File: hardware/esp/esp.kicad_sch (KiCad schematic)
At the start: 41 parts, among them J1 USB_C_Receptacle_USB2.0_16P, J2 Conn_01x02, J3 USB_C_Receptacle_USB2.0_16P, J4 Conn_01x02, Q1 PNP, Q2 PNP, Q3 PNP, Q4 PNP, SW1 RESET, SW2 BOOT, U1 AMS1117-3.3, U2 ESP32-S3-WROOM-1, U6 CP2102N-Axx-xQFN20

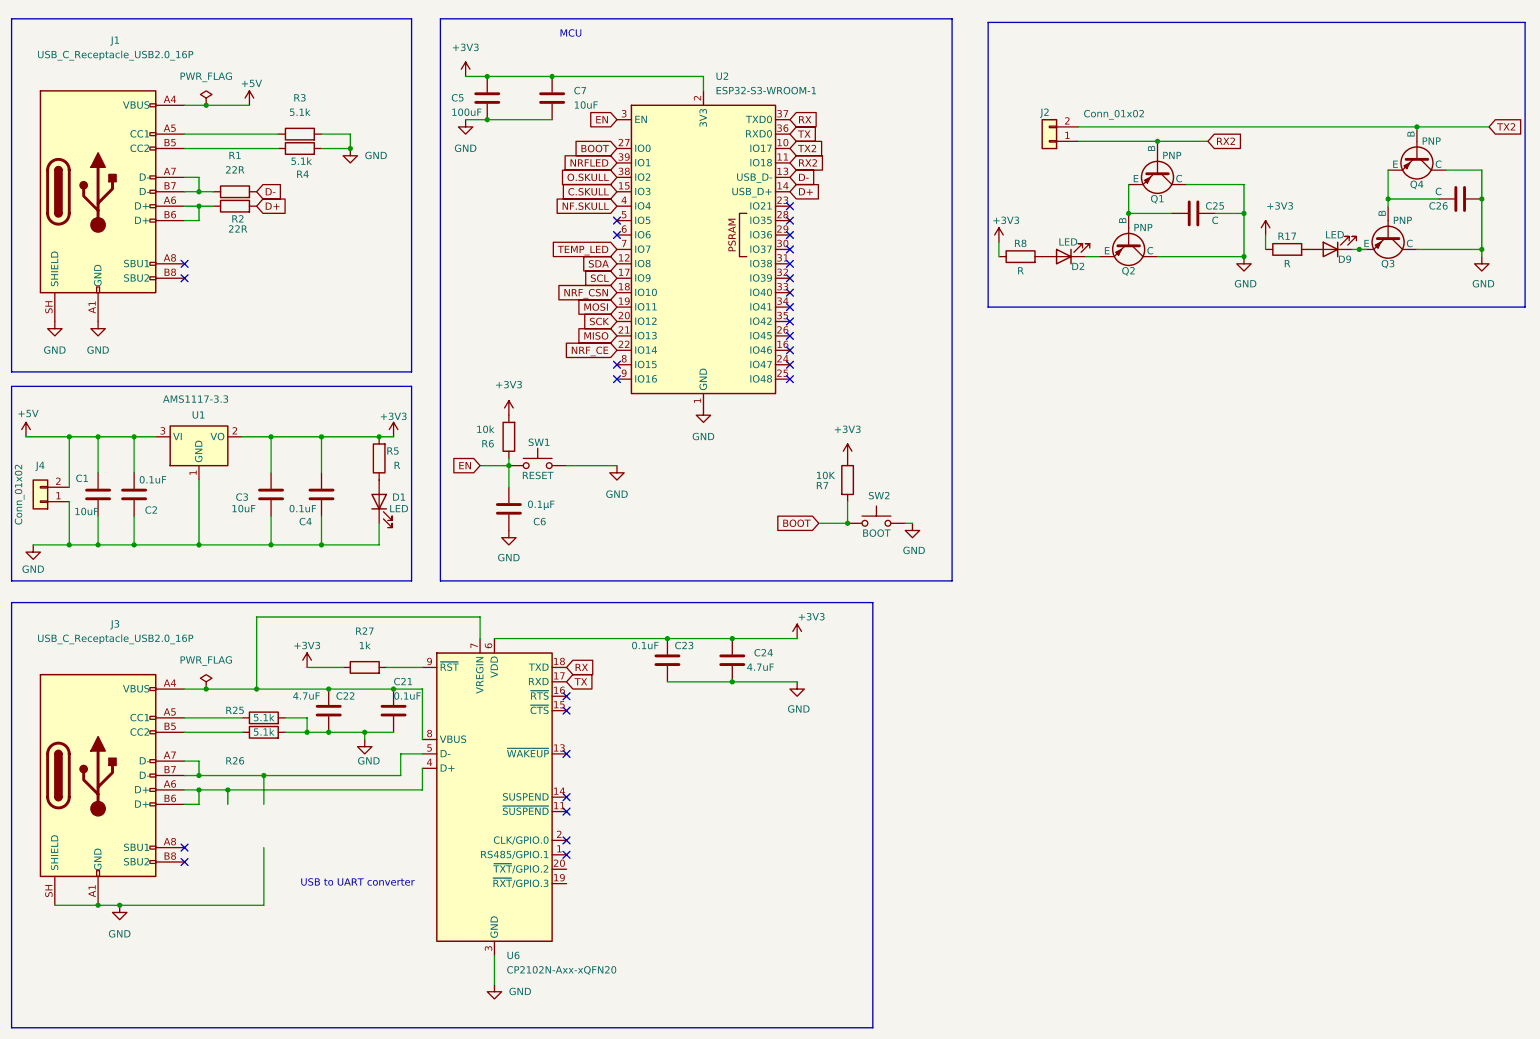
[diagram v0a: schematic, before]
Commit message: Placing Bidirectional TVS diodes and fixing schematic + placing components on pcb
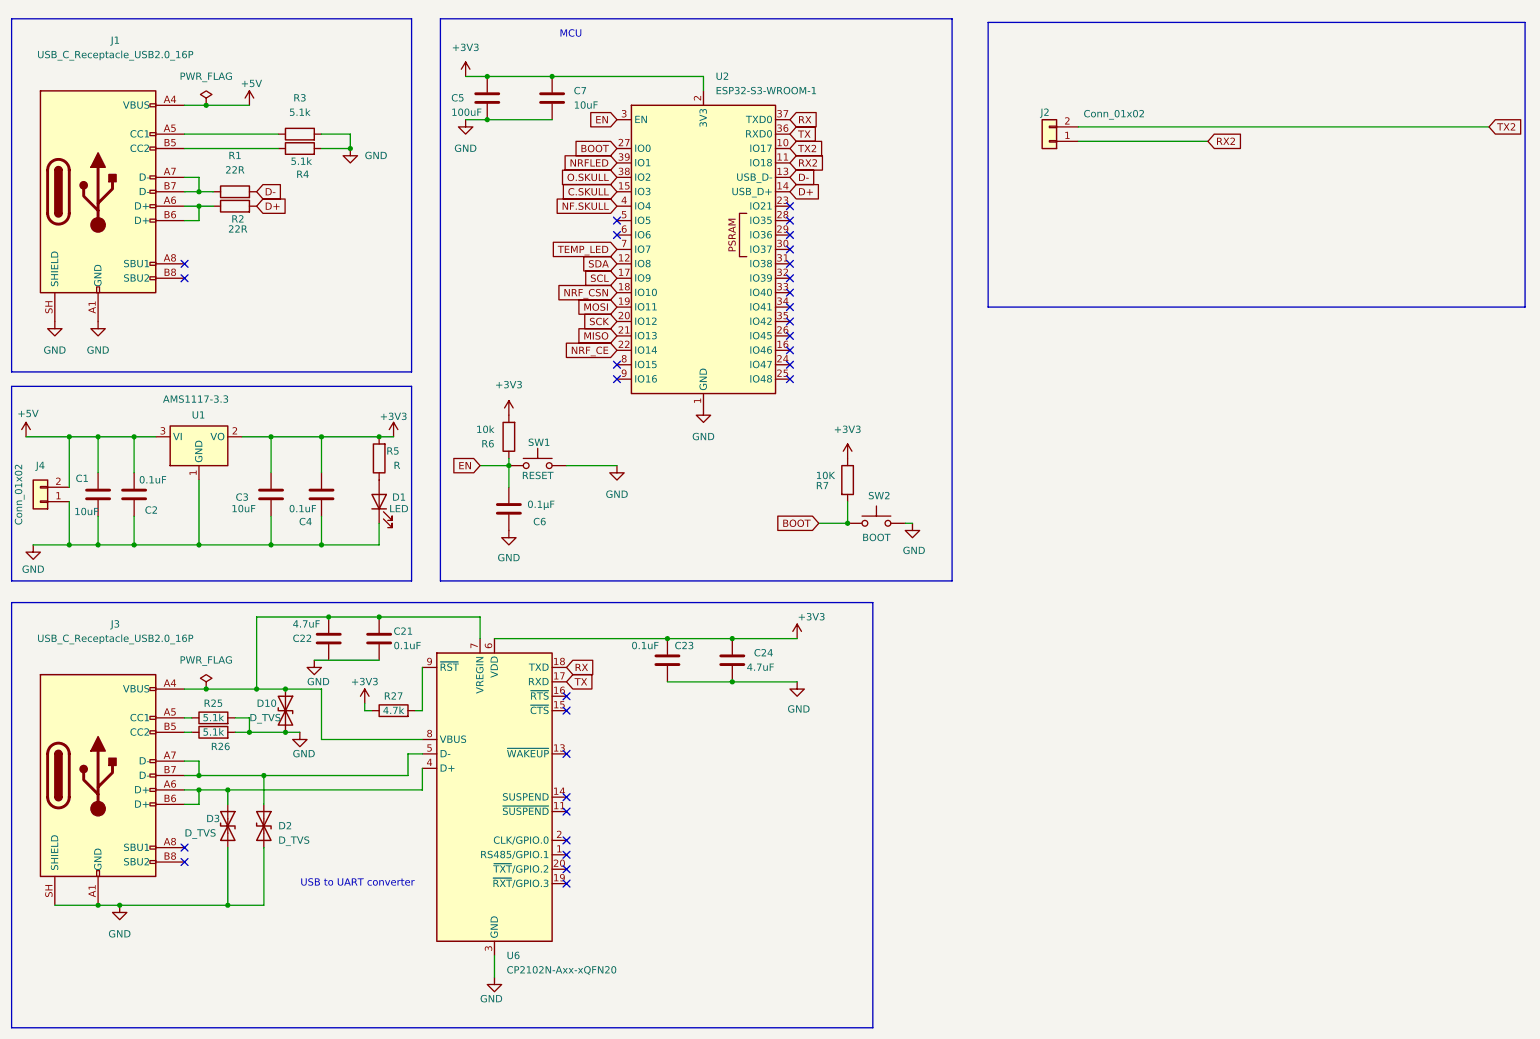
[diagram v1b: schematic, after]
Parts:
- removed C25, C26: C, Capacitor_SMD:C_0805_2012Metric, symbol Device:C
- removed D2, D9: LED, LED_SMD:LED_0603_1608Metric, symbol Device:LED
- removed Q1, Q2, Q3, Q4: PNP, symbol Simulation_SPICE:PNP
- removed R17, R8: R, Resistor_SMD:R_0805_2012Metric, symbol Device:R
- added D10, D2, D3: D_TVS, Diode_SMD:D_SOD-123, symbol Device:D_TVS
- R27: value 1k -> 4.7k
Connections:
- net GND: now also D10.2 (A2), D2.2 (A2), D3.2 (A2); no longer C22.2
- net at C21.1, C22.1, J3.A4 (VBUS)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: now also D10.1 (A1)
- net at J3.A6 (D+), J3.B6 (D+), U6.4 (D+): now also D3.1 (A1)
- net at J3.A7 (D-), J3.B7 (D-), U6.5 (D-): now also D2.1 (A1)
- no-connect marks 28 -> 30
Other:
- moved on the sheet: C21, C22, R25, R26, R27

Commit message: Updating pins, and scehmatic
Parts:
- renumbered C23 to C10, C24 to C11, C22 to C5, C21 to C6, C5 to C7, C6 to C8, C7 to C9, D3 to D1, D10 to D3, D1 to D4, J4 to J1, J1 to J2, J2 to J4, R25 to R1, R7 to R10, R26 to R2, R1 to R3, R2 to R4, R3 to R5, R4 to R6, R5 to R7, R27 to R8, R6 to R9, U6 to U2, U2 to U3
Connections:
- net GND is gone; now on net +3V3: C1.2, C10.2, C11.2, C2.2, C3.2, C4.2, C6.2, C7.1, C8.1, C9.1, D1.2 (A2), D2.2 (A2), D3.2 (A2), D4.1 (K), J1.1 (Pin_1), J2.A1 (GND), J2.A12 (GND), J2.B1 (GND), J2.B12 (GND), J2.SH (SHIELD), J3.A1 (GND), J3.A12 (GND), J3.B1 (GND), J3.B12 (GND), J3.SH (SHIELD), R1.2, R2.2, R5.2, R6.2, SW1.2, SW2.2, U1.1 (GND), U2.12 (GND), U2.21 (GND), U2.3 (GND), U3.1 (GND), U3.40 (GND), U3.41 (GND)
- net +3V3: now also C5.2
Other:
- moved on the sheet: C1, C10, C11, C2, C3, C4, C5, C6, C7, C8, C9, D1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

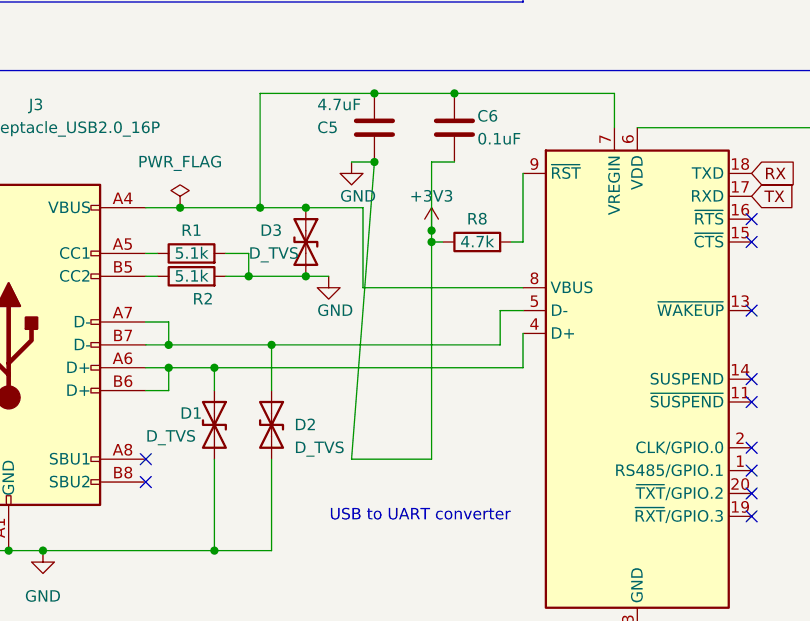
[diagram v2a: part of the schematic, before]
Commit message: Fixing schematic error and routing PCB
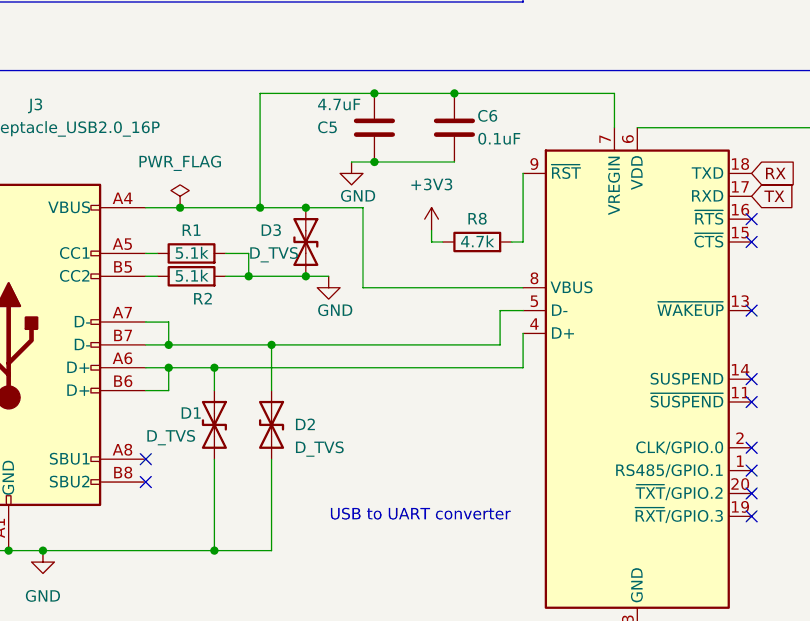
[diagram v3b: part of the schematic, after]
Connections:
- net +3V3: no longer C1.2, C10.2, C11.2, C2.2, C3.2, C4.2, C5.2, C6.2, C7.1, C8.1, C9.1, D1.2 (A2), D2.2 (A2), D3.2 (A2), D4.1 (K), J1.1 (Pin_1), J2.A1 (GND), J2.A12 (GND), J2.B1 (GND), J2.B12 (GND), J2.SH (SHIELD), J3.A1 (GND), J3.A12 (GND), J3.B1 (GND), J3.B12 (GND), J3.SH (SHIELD), R1.2, R2.2, R5.2, R6.2, SW1.2, SW2.2, U1.1 (GND), U2.12 (GND), U2.21 (GND), U2.3 (GND), U3.1 (GND), U3.40 (GND), U3.41 (GND)
- new net GND: C1.2, C10.2, C11.2, C2.2, C3.2, C4.2, C5.2, C6.2, C7.1, C8.1, C9.1, D1.2 (A2), D2.2 (A2), D3.2 (A2), D4.1 (K), J1.1 (Pin_1), J2.A1 (GND), J2.A12 (GND), J2.B1 (GND), J2.B12 (GND), J2.SH (SHIELD), J3.A1 (GND), J3.A12 (GND), J3.B1 (GND), J3.B12 (GND), J3.SH (SHIELD), R1.2, R2.2, R5.2, R6.2, SW1.2, SW2.2, U1.1 (GND), U2.12 (GND), U2.21 (GND), U2.3 (GND), U3.1 (GND), U3.40 (GND), U3.41 (GND)
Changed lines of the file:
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@@
 	)
 	(junction
-		(at 81.28 101.6)
+		(at 74.93 93.98)
 		(diameter 0)
 		(color 0 0 0 0)
@@
 	)
 	(junction
-		(at 74.93 93.98)
-		(diameter 0)
-		(color 0 0 0 0)
-	)
-	(junction
 		(at 120.65 45.72)
 		(diameter 0)
@@
 	)
 	(junction
-		(at 81.28 102.87)
-		(diameter 0)
-		(color 0 0 0 0)
-	)
-	(junction
 		(at 83.82 86.36)
 		(diameter 0)
@@
 	(wire
 		(pts
-			(xy 81.28 93.98) (xy 81.28 101.6)
-		)
-		(stroke
-			(width 0)
-			(type default)
-		)
-	)
-	(wire
-		(pts
 			(xy 73.66 99.06) (xy 67.31 99.06)
 		)
@@
 	(wire
 		(pts
-			(xy 81.28 93.98) (xy 83.82 93.98)
+			(xy 74.93 93.98) (xy 83.82 93.98)
 		)
 		(stroke
@@
 	(wire
 		(pts
-			(xy 81.28 127) (xy 72.39 127)
-		)
-		(stroke
-			(width 0)
-			(type default)
-		)
-	)
-	(wire
-		(pts
 			(xy 63.5 127) (xy 63.5 137.16)
 		)
@@
 	(wire
 		(pts
-			(xy 81.28 102.87) (xy 81.28 127)
-		)
-		(stroke
-			(width 0)
-			(type default)
-		)
-	)
-	(wire
-		(pts
 			(xy 198.12 95.25) (xy 198.12 100.33)
 		)
@@
 	(wire
 		(pts
-			(xy 74.93 93.98) (xy 72.39 127)
-		)
-		(stroke
-			(width 0)
-			(type default)
-		)
-	)
-	(wire
-		(pts
 			(xy 67.31 99.06) (xy 62.23 99.06)
 		)
@@
 		)
 		(property "Value" "+3V3"
-			(at 81.28 97.79 0)
+			(at 81.28 96.52 0)
 			(show_name no)
 			(do_not_autoplace no)

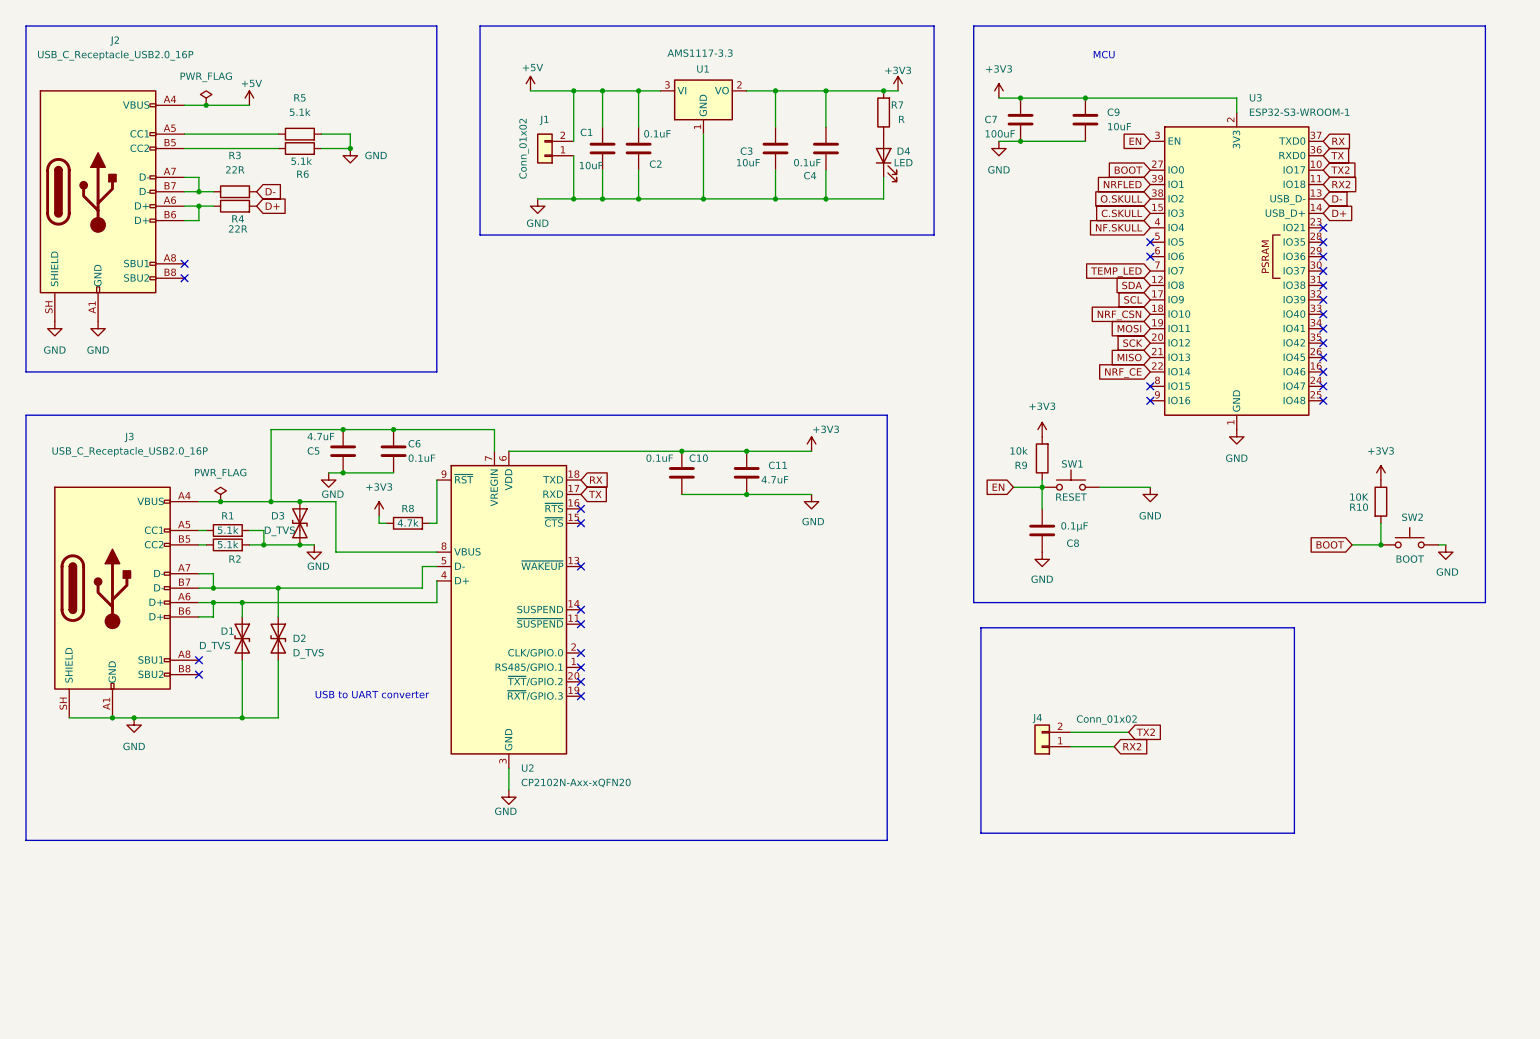
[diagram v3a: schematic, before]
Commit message: Modifiying schematic after schematic review
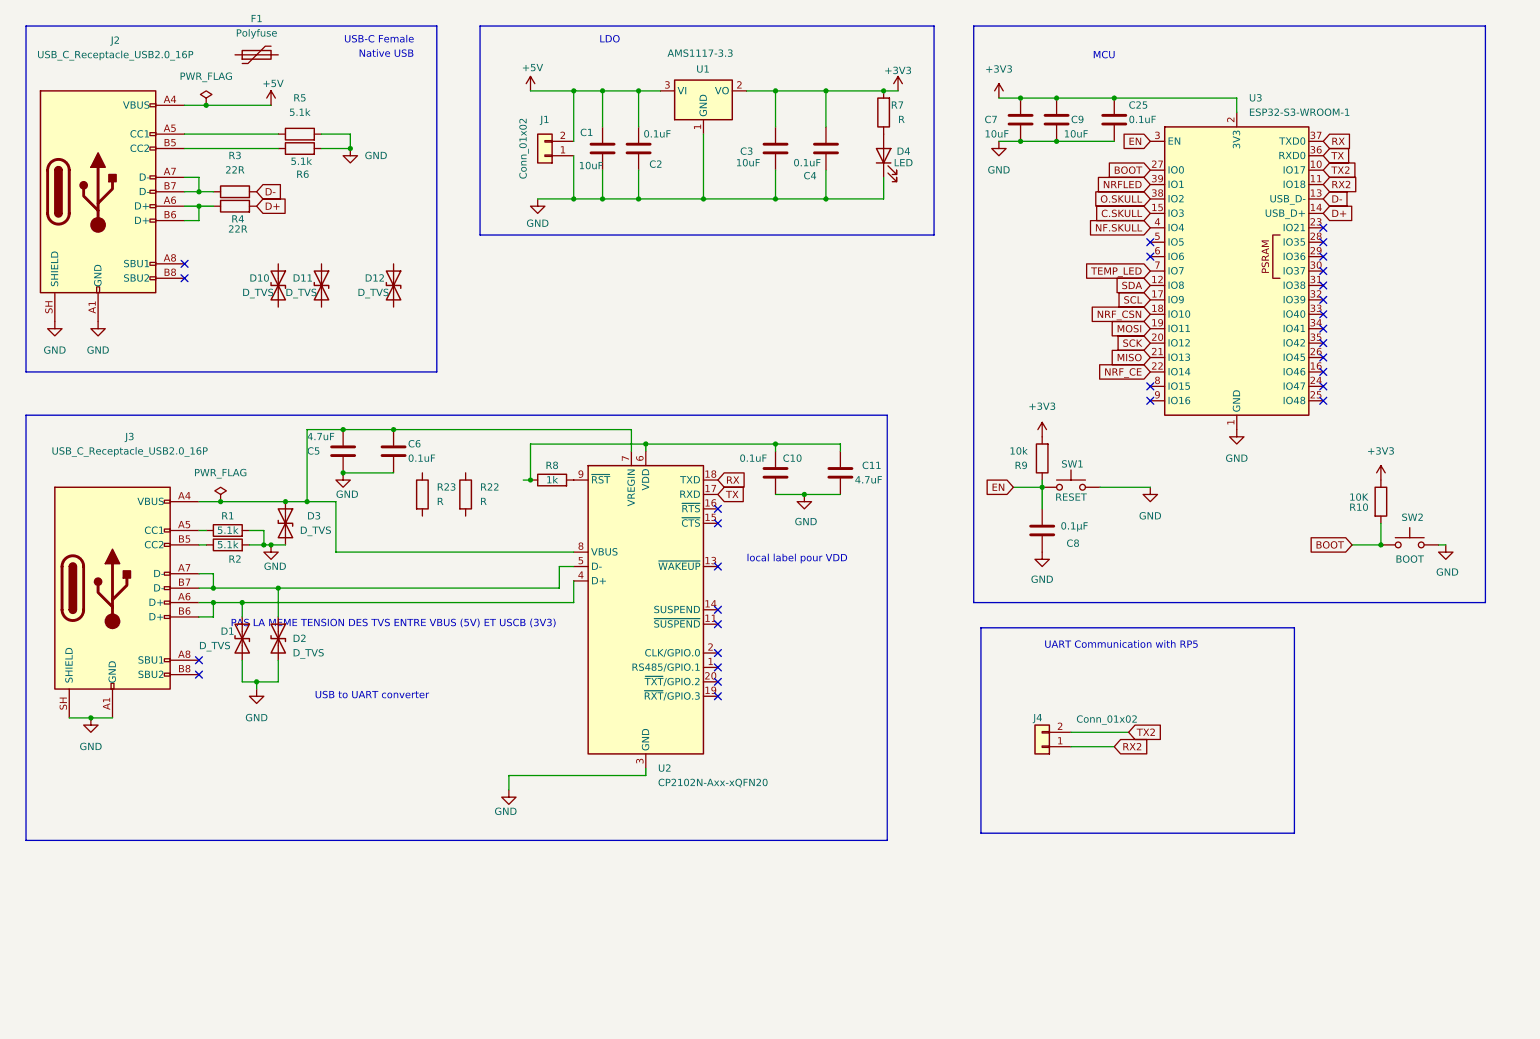
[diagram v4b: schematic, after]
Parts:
- added C25: 0.1uF, Capacitor_SMD:C_0805_2012Metric, symbol Device:C
- added D10, D11, D12: D_TVS, Diode_SMD:D_SOD-123, symbol Device:D_TVS
- added F1: Polyfuse, symbol Device:Polyfuse
- added R22, R23: R, symbol Device:R
- C7: value 100uF -> 10uF
- R8: value 4.7k -> 1k
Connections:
- net +3V3: now also C25.2; no longer C10.1, C11.1, R8.1, U2.6 (VDD)
- net GND: now also C25.1
- new net: C10.1, C11.1, R8.1, U2.6 (VDD)
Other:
- note added: "LDO"
- note added: "Native USB"
- note added: "PAS LA MEME TENSION DES TVS ENTRE VBUS (5V) ET USCB (3V3)"
- note added: "UART Communication with RP5"
- note added: "USB-C Female"
- note added: "local label pour VDD"
- moved on the sheet: C10, C11, C9, D3, R8, U2
